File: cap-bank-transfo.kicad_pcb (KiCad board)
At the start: 2 copper layers, 110 x 50 mm, 25 parts, among them J1 Screw_Terminal_01x02, J2 Screw_Terminal_01x02, J3 Screw_Terminal_01x02, T1 FS28-420

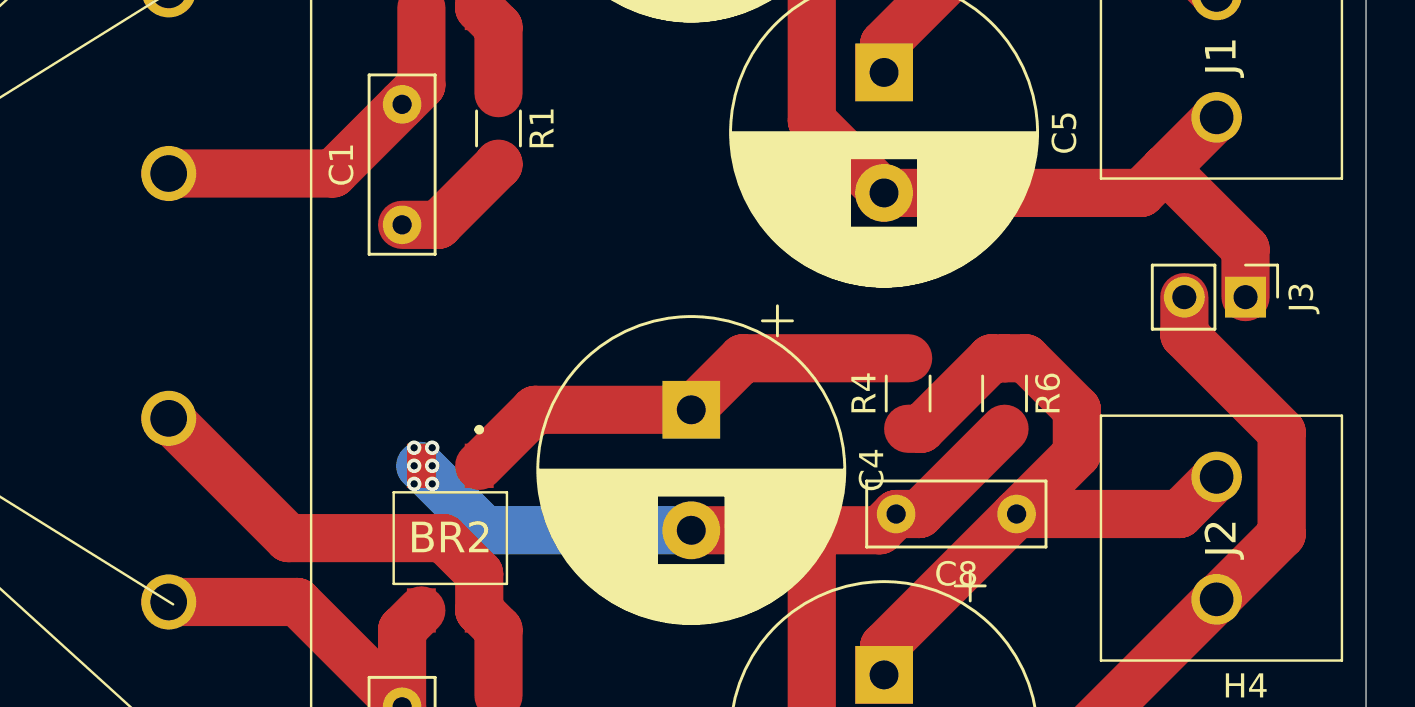
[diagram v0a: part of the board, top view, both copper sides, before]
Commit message: added second header for ground jumpers
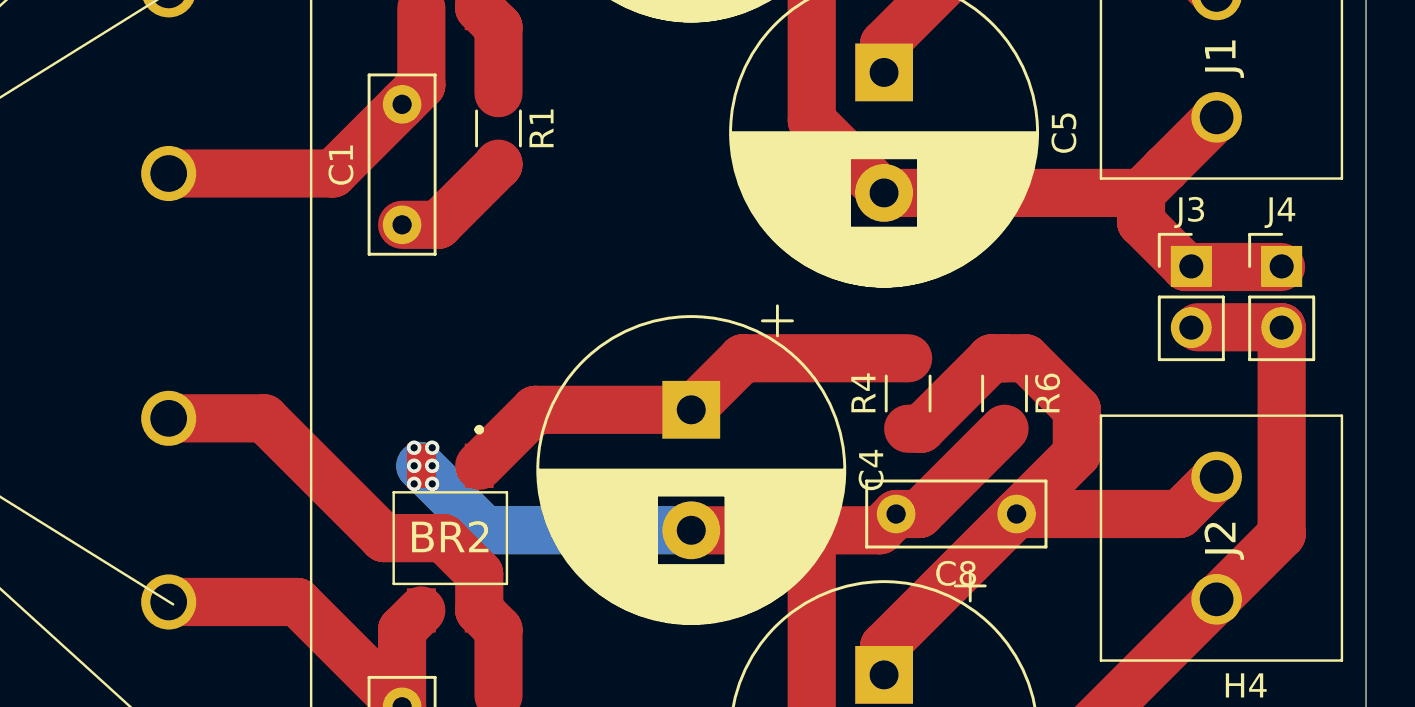
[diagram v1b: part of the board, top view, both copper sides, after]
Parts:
- added J4: Screw_Terminal_01x02, Connector_PinHeader_2.54mm:PinHeader_1x02_P2.54mm_Vertical, F.Cu at (181.5, 68.7)
- moved J3 2.59 mm to (177.8, 68.7), turned to 0 degrees
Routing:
- net gnd_1: track 61.7 -> 62.8 mm
- net gnd_2: track 71.8 -> 72.4 mm
